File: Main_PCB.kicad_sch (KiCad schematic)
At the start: 5 parts

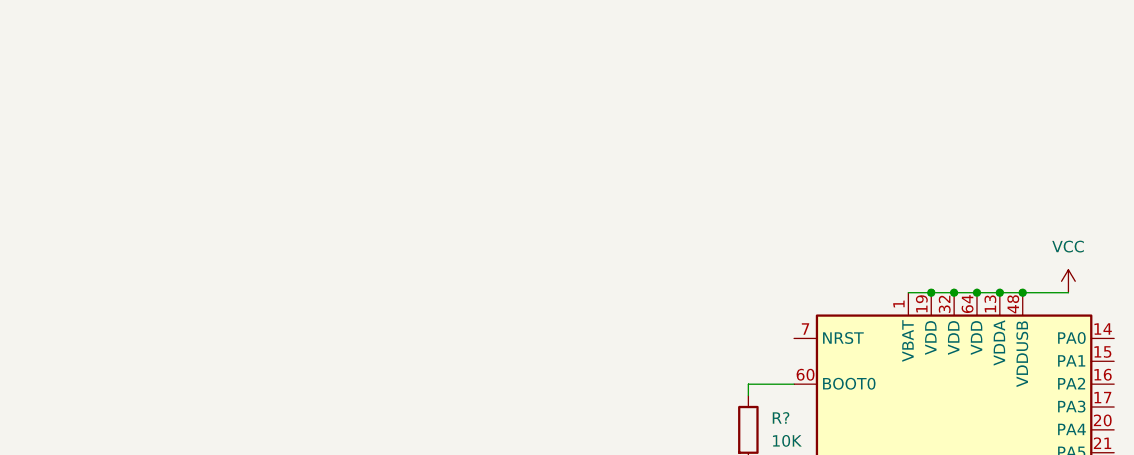
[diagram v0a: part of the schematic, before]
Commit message: started microcontroller pcb added lora, EEPROM, ArduinoHeaders and OUTPUTPINS
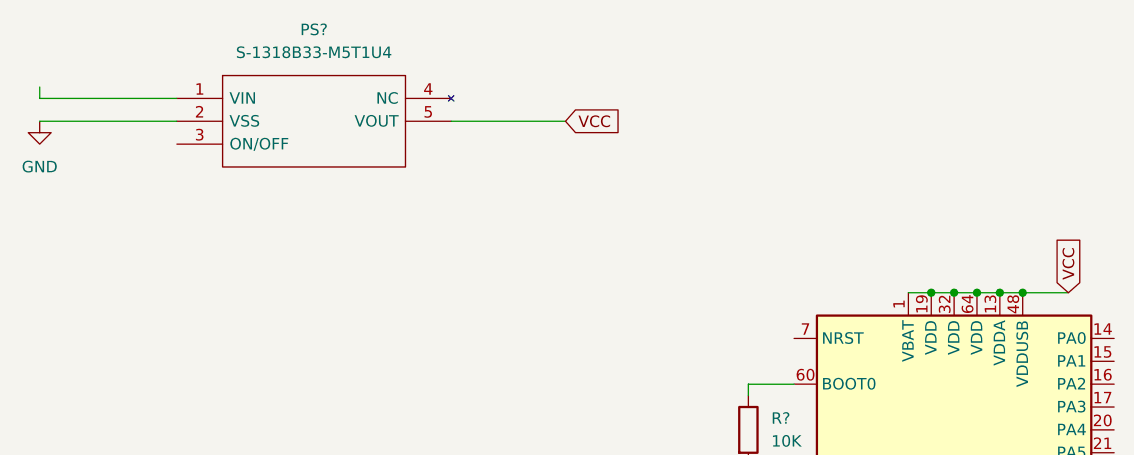
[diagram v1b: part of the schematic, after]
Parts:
- added PS?: S-1318B33-M5T1U4, SOT95P275X130-5N, symbol S-1318B33-M5T1U4:S-1318B33-M5T1U4
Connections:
- net GND: now also PS?.2 (VSS)
- net VCC: now also PS?.5 (VOUT)
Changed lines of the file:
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@@
   (junction (at 154.94 146.05) (diameter 0.9144) (color 0 0 0 0))
   (junction (at 157.48 54.61) (diameter 0.9144) (color 0 0 0 0))
+  (wire (pts (xy 48.26 31.75) (xy 48.26 33.02))
+    (stroke (width 0) (type default) (color 0 0 0 0))
+  )
+  (wire (pts (xy 48.26 33.02) (xy 63.5 33.02))
+    (stroke (width 0) (type default) (color 0 0 0 0))
+  )
+  (wire (pts (xy 63.5 35.56) (xy 48.26 35.56))
+    (stroke (width 0) (type default) (color 0 0 0 0))
+  )
+  (wire (pts (xy 93.98 35.56) (xy 106.68 35.56))
+    (stroke (width 0) (type default) (color 0 0 0 0))
+  )
   (wire (pts (xy 115.57 138.43) (xy 115.57 146.05))
     (stroke (width 0) (type solid) (color 0 0 0 0))
@@
     (stroke (width 0) (type solid) (color 0 0 0 0))
   )
-  (symbol (lib_id "power:VCC") (at 162.56 54.61 0) (unit 1)
-    (in_bom yes) (on_board yes) (fields_autoplaced)
-    (property "Reference" "#PWR?" (id 0) (at 162.56 58.42 0)
-      (effects (font (size 1.27 1.27)) hide)
-    )
-    (property "Value" "VCC" (id 1) (at 162.56 49.53 0))
-    (property "Footprint" "" (id 2) (at 162.56 54.61 0)
-      (effects (font (size 1.27 1.27)) hide)
-    )
-    (property "Datasheet" "" (id 3) (at 162.56 54.61 0)
+  (global_label "VCC" (shape input) (at 106.68 35.56 0) (fields_autoplaced)
+    (effects (font (size 1.27 1.27)) (justify left))
+    (property "Intersheet References" "${INTERSHEET_REFS}" (id 0) (at 112.7217 35.4806 0)
+      (effects (font (size 1.27 1.27)) (justify left) hide)
+    )
+  )
+  (global_label "VCC" (shape input) (at 162.56 54.61 90) (fields_autoplaced)
+    (effects (font (size 1.27 1.27)) (justify left))
+    (property "Intersheet References" "${INTERSHEET_REFS}" (id 0) (at 162.4806 48.5683 90)
+      (effects (font (size 1.27 1.27)) (justify left) hide)
+    )
+  )
+  (symbol (lib_id "power:GND") (at 48.26 35.56 0) (unit 1)
+    (in_bom yes) (on_board yes) (fields_autoplaced)
+    (property "Reference" "#PWR?" (id 0) (at 48.26 41.91 0)
+      (effects (font (size 1.27 1.27)) hide)
+    )
+    (property "Value" "GND" (id 1) (at 48.26 40.64 0))
+    (property "Footprint" "" (id 2) (at 48.26 35.56 0)
+      (effects (font (size 1.27 1.27)) hide)
+    )
+    (property "Datasheet" "" (id 3) (at 48.26 35.56 0)
       (effects (font (size 1.27 1.27)) hide)
     )
@@
     (pin "1")
     (pin "2")
+  )
+  (symbol (lib_id "S-1318B33-M5T1U4:S-1318B33-M5T1U4") (at 63.5 33.02 0) (unit 1)
+    (in_bom yes) (on_board yes) (fields_autoplaced)
+    (property "Reference" "PS?" (id 0) (at 78.74 25.4 0))
+    (property "Value" "S-1318B33-M5T1U4" (id 1) (at 78.74 27.94 0))
+    (property "Footprint" "SOT95P275X130-5N" (id 2) (at 90.17 30.48 0)
+      (effects (font (size 1.27 1.27)) (justify left) hide)
+    )
+    (property "Datasheet" "https://componentsearchengine.com/Datasheets/1/S-1318B33-M5T1U4.pdf" (id 3) (at 90.17 33.02 0)
+      (effects (font (size 1.27 1.27)) (justify left) hide)
+    )
+    (property "Description" "LDO Voltage Regulators 5.5V Input 100mA 95 nA 3.3V Output" (id 4) (at 90.17 35.56 0)
+      (effects (font (size 1.27 1.27)) (justify left) hide)
+    )
+    (property "Height" "1.3" (id 5) (at 90.17 38.1 0)
+      (effects (font (size 1.27 1.27)) (justify left) hide)
+    )
+    (property "Manufacturer_Name" "ABLIC Inc." (id 6) (at 90.17 40.64 0)
+      (effects (font (size 1.27 1.27)) (justify left) hide)
+    )
+    (property "Manufacturer_Part_Number" "S-1318B33-M5T1U4" (id 7) (at 90.17 43.18 0)
+      (effects (font (size 1.27 1.27)) (justify left) hide)
+    )
+    (property "Mouser Part Number" "628-S-1318B33-M5T1U4" (id 8) (at 90.17 45.72 0)
+      (effects (font (size 1.27 1.27)) (justify left) hide)
+    )
+    (property "Mouser Price/Stock" "https://www.mouser.com/Search/Refine.aspx?Keyword=628-S-1318B33-M5T1U4" (id 9) (at 90.17 48.26 0)
+      (effects (font (size 1.27 1.27)) (justify left) hide)
+    )
+    (property "Arrow Part Number" "" (id 10) (at 90.17 50.8 0)
+      (effects (font (size 1.27 1.27)) (justify left) hide)
+    )
+    (property "Arrow Price/Stock" "" (id 11) (at 90.17 53.34 0)
+      (effects (font (size 1.27 1.27)) (justify left) hide)
+    )
+    (pin "1")
+    (pin "2")
+    (pin "3")
+    (pin "4")
+    (pin "5")
   )
   (symbol (lib_id "MCU_ST_STM32L4:STM32L476RGTx") (at 149.86 100.33 0) (unit 1)
@@
       (reference "#PWR?") (unit 1) (value "GND") (footprint "")
     )
-    (path "/3cdf3227-f30a-4495-ac8b-0d36e0f57fd9"
-      (reference "#PWR?") (unit 1) (value "VCC") (footprint "")
-    )
     (path "/4c2bd4ea-05fe-490a-aef5-37b9aa28a49f"
       (reference "#PWR?") (unit 1) (value "GND") (footprint "")
     )
     (path "/71f3acb8-f249-4477-8678-d418f3c6a7d2"
+      (reference "#PWR?") (unit 1) (value "GND") (footprint "")
+    )
+    (path "/7621adb7-fe8e-4a06-9c81-43b3d705b253"
       (reference "#PWR?") (unit 1) (value "GND") (footprint "")
     )
@@
       (reference "C?") (unit 1) (value "4pF") (footprint "Capacitor_SMD:C_0603_1608Metric_Pad1.08x0.95mm_HandSolder")
     )
+    (path "/7fb52c71-aeae-4a20-8c17-b92ca4f2d7cf"
+      (reference "PS?") (unit 1) (value "S-1318B33-M5T1U4") (footprint "SOT95P275X130-5N")
+    )
     (path "/f64992af-738a-4402-854b-85b02260bd48"

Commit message: fixed microcontroller
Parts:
- added A?: Arduino_UNO_R3, Module:Arduino_UNO_R3, symbol MCU_Module:Arduino_UNO_R3
- added C? (x2): 100nF, symbol Device:C
- added IC?: 24AA64T-I_OT, SOT95P270X145-5N, symbol 24AA64T-I_OT:24AA64T-I_OT
- added IC?: TCN75AVUA713-VAO, SOP65P490X110-8N, symbol TCN75AVUA713-VAO:TCN75AVUA713-VAO
- added J?: Conn_02x03_Odd_Even, symbol Connector_Generic:Conn_02x03_Odd_Even
- added J?: Conn_Coaxial, symbol Connector:Conn_Coaxial
- added LED?: IN-P55TATRGB, INP55TATRGB, symbol IN-P55TATRGB:IN-P55TATRGB
- added R1, R?: 0R, symbol Device:R
- added R?: 4.7KR, symbol Device:R
- added U?: LTR-329ALS-01, LTR329ALS01, symbol LTR-329ALS-01:LTR-329ALS-01
- added U?: RFM95W-868S2, symbol RF_Module:RFM95W-868S2
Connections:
- net GND: now also A?.29 (GND), A?.6 (GND), A?.7 (GND), C?.1, C?.1, IC?.2 (VSS), IC?.4 (GND), IC?.5 (A2), IC?.6 (A1), J?.1 (Pin_1), J?.2 (Ext), U?.1 (GND), U?.10 (GND), U?.2 (GND), U?.8 (GND)
- net VCC: now also A?.4 (3V3), C?.2, C?.2, IC?.4 (VCC), IC?.7 (A0), IC?.8 (VDD), J?.2 (Pin_2), R?.1, U?.1 (VDD), U?.13 (3.3V)
- net OSC32_IN: now reaches C?.1, U?.3 (PC14), Y?.1
- net OSC32_OUT: now reaches C?.1, U?.4 (PC15), Y?.2
- net VBAT: now reaches PS?.1 (VIN)
- net VBAT: now also R1.1
- net at PS?.3 (ON/OFF): now also R1.2
- net SPI_LORA_NSS: now reaches U?.14 (PA0)
- net SPI_LORA_NSS: now also A?.9 (A0), U?.5 (NSS)
- net Lora-Reset: now reaches U?.15 (PA1)
- net Lora-Reset: now also A?.10 (A1), R?.2
- net SPI_LORA_SCK: now reaches U?.21 (PA5)
- net SPI_LORA_SCK: now also A?.28 (D13), U?.4 (SCK)
- net SPI_LORA_MISO: now reaches U?.22 (PA6)
- net SPI_LORA_MISO: now also A?.27 (D12), U?.2 (MISO)
- net SPI_LORA_MOSI: now reaches U?.23 (PA7)
- net SPI_LORA_MOSI: now also A?.26 (D11), U?.3 (MOSI)
- net IC2_MoistureSensor_SCL2: now reaches U?.34 (PB13)
- net IC2_MoistureSensor_SCL2: now also J?.5 (Pin_5)
- net IC2_MoistureSensor_SDA2: now reaches U?.35 (PB14)
- net IC2_MoistureSensor_SDA2: now also J?.6 (Pin_6)
- net LORA_DIO0: now reaches U?.43 (PA10)
- net LORA_DIO0: now also A?.17 (D2), U?.14 (DIO0)
- net LORA_DIO1: now reaches U?.55 (PB3)
- net LORA_DIO1: now also A?.18 (D3), U?.15 (DIO1)
- net I2C_EEPROM_SDA: now reaches U?.59 (PB7)
- net I2C_EEPROM_SDA: now also IC?.3 (SDA)
- net I2C_EEPROM_SCL: now reaches U?.61 (PB8)
- net I2C_EEPROM_SCL: now also IC?.1 (SCL)
- net IC2_MoistureSensor_SCL1: now reaches U?.8 (PC0)
- net IC2_MoistureSensor_SCL1: now also IC?.2 (SCL), J?.3 (Pin_3), U?.4 (SCL)
- net IC2_MoistureSensor_SDA1: now reaches U?.9 (PC1)
- net IC2_MoistureSensor_SDA1: now also IC?.1 (SDA), J?.4 (Pin_4), U?.3 (SDA)
- new net: J?.1 (In), U?.9 (ANT)
- new net: R?.1, R?.2, U?.6 (RESET)
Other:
- note added: "ARDUINO HEADERS"
- note added: "Cystal"
- note added: "EEPROM"
- note added: "LICHTSENSOR_MAIN_BOARD"
- note added: "LORA"
- note added: "OUTPUT_PINS_MOISTURE"
- note added: "TEMPERATUURSENSOR_MAIN_BOARD"
- note added: "Voeding"
- moved on the sheet: C?, PS?, R?, U?, Y?

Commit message: added connector for moisture sensor + connected arduino header 2 microcontroller
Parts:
- added R? (x3): 470R, symbol Device:R
- gave numbers to parts that had none: 1
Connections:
- net GND: now also LED?.1 (CATHODE_BLUE), LED?.2 (CATHODE_RED), LED?.3 (CATHODE_GREEN)
- net IC2_MoistureSensor_SCL1: now also A?.14 (SCL/A5), A?.32 (SCL/A5)
- net IC2_MoistureSensor_SDA1: now also A?.13 (SDA/A4), A?.31 (SDA/A4)
- net VCC: now also A?.2 (IOREF), A?.30 (AREF)
- net at LED?.4 (ANODE_GREEN): now also R?.2
- net at LED?.5 (ANODE_RED): now also R?.2
- net at LED?.6 (ANODE_BLUE): now also R?.2
- net D1_TX: now reaches U?.16 (PA2)
- net D1_TX: now also A?.16 (D1/TX)
- net D0_TX: now reaches U?.17 (PA3)
- net D0_TX: now also A?.15 (D0/RX)
- net A2: now reaches U?.20 (PA4)
- net A2: now also A?.11 (A2)
- net A3: now reaches U?.26 (PB0)
- net A3: now also A?.12 (A3)
- net D6: now reaches U?.29 (PB10)
- net D6: now also A?.21 (D6)
- net D9: now reaches U?.38 (PC7)
- net D9: now also A?.24 (D9)
- net D7: now reaches U?.41 (PA8)
- net D7: now also A?.22 (D7)
- net D8: now reaches U?.42 (PA9)
- net D8: now also A?.23 (D8)
- net D5: now reaches U?.56 (PB4)
- net D5: now also A?.20 (D5)
- net D4: now reaches U?.57 (PB5)
- net D4: now also A?.19 (D4)
- net D10: now reaches U?.58 (PB6)
- net D10: now also A?.25 (D10)
- net Reset: now reaches U?.7 (NRST)
- net Reset: now also A?.3 (~{RESET})
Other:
- note added: "INDICATIE_LED"
- note added: "Voeding LDO"
- note removed: "Voeding"
- moved on the sheet: A?, C?, IC?, J1, J?, LED?, PS?, R1, R?, U?, Y?

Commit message: added battery holder and swd programming port
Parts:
- removed LED?: IN-P55TATRGB, INP55TATRGB, symbol IN-P55TATRGB:IN-P55TATRGB
- removed R? (x3): 470R, symbol Device:R
- added F1: Fuse, Fuse:Fuse_0603_1608Metric_Pad1.05x0.95mm_HandSolder, symbol Device:Fuse
- added JP1: 20021521-00010T1LF, 20021521-00010T1LF:20021521-00010T1LF, symbol SWD_header:20021521-00010T1LF
- added U3: Dual_AA, Dual_AA:Dual_AA, symbol New_Library:Dual_AA
- gave numbers to parts that had none: 16
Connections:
- net GND: now also JP1.3, JP1.5, JP1.9, U3.3 (-bat1), U3.4 (-bat2)
- net LORA_DIO1: now also U4.28 (PB2); no longer U4.55 (PB3)
- net Reset: now also JP1.10
- net VBAT: now also F1.1
- net VCC: now also JP1.1
- net SWDIO: now reaches U4.46 (PA13)
- net SWDIO: now also JP1.2
- net SWCLK: now reaches U4.49 (PA14)
- net SWCLK: now also JP1.4
- new net: F1.2, U3.1 (+bat1), U3.2 (+bat2)
- new net SWO: JP1.6, U4.55 (PB3)
- no-connect marks 0 -> 3
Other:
- note added: "battery holder"
- note added: "swd programming port"
- note removed: "INDICATIE_LED"

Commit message: assigned footprints
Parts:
- added C10, C11, C12, C13, C14, C15, C5, C6, C7, C8, C9, C?: 100nF, Capacitor_SMD:C_0603_1608Metric_Pad1.08x0.95mm_HandSolder, symbol Device:C
- C1, C2: footprint (none) -> Capacitor_SMD:C_0603_1608Metric_Pad1.08x0.95mm_HandSolder
- IC1: footprint SOP65P490X110-8N -> TCN75AVUA713-VAO:SOP65P490X110-8N
- IC2: footprint SOT95P270X145-5N -> 24AA64T-I_OT:SOT95P270X145-5N
- J2: footprint (none) -> Connector_IDC:IDC-Header_2x03_P2.54mm_Vertical
- PS1: footprint SOT95P275X130-5N -> S-1318B33:SOT95P275X130-5N
- R1, R2, R3, R7: footprint (none) -> Resistor_SMD:R_0603_1608Metric_Pad0.98x0.95mm_HandSolder
- U1: footprint LTR329ALS01 -> KiCad:LTR329ALS01
- U2: footprint (none) -> RFM95W-868S2:XCVR_RFM95W-868S2
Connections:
- net GND: now also C10.1, C11.1, C12.1, C13.1, C14.1, C15.1, C5.1, C6.1, C7.1, C8.1, C9.1, C?.1
- net VBAT: now also C14.2
- net VCC: now also C10.2, C11.2, C12.2, C13.2, C15.2, C5.2, C6.2, C7.2, C8.2, C9.2, C?.2
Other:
- moved on the sheet: C3, C4, Y1

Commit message: did alot of the routing and pcb layout
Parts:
- removed A1: Arduino_UNO_R3, Module:Arduino_UNO_R3, symbol MCU_Module:Arduino_UNO_R3
- removed U3: Dual_AA, Dual_AA:Dual_AA, symbol New_Library:Dual_AA
- added C17, C18, C19, C20: 100nF, Capacitor_SMD:C_0805_2012Metric_Pad1.18x1.45mm_HandSolder, symbol Device:C
- added D1: LED, LED_SMD:LED_0805_2012Metric_Pad1.15x1.40mm_HandSolder, symbol Device:LED
- added F2: Fuse, Fuse:Fuse_0603_1608Metric_Pad1.05x0.95mm_HandSolder, symbol Device:Fuse
- added J3: USB_C_Receptacle_USB2.0, Connector_USB:USB_C_Receptacle_HRO_TYPE-C-31-M-12, symbol Connector:USB_C_Receptacle_USB2.0
- added J4: Conn_01x03_Male, Connector_PinHeader_2.54mm:PinHeader_1x03_P2.54mm_Vertical, symbol Connector:Conn_01x03_Male
- added J? (x2): Conn_01x15_Female, symbol Connector:Conn_01x15_Female
- added PS2: S-1318B33-M5T1U4, S-1318B33:SOT95P275X130-5N, symbol S-1318B33-M5T1U4:S-1318B33-M5T1U4
- added R10, R6: 360R, Resistor_SMD:R_0603_1608Metric_Pad0.98x0.95mm_HandSolder, symbol Device:R
- added R11: 0R, Resistor_SMD:R_0603_1608Metric_Pad0.98x0.95mm_HandSolder, symbol Device:R
- added R12: 220k, Resistor_SMD:R_0603_1608Metric_Pad0.98x0.95mm_HandSolder, symbol Device:R
- added R13: 330k, Resistor_SMD:R_0603_1608Metric_Pad0.98x0.95mm_HandSolder, symbol Device:R
- added R4, R5: 5.1k, Resistor_SMD:R_0603_1608Metric_Pad0.98x0.95mm_HandSolder, symbol Device:R
- added R8, R9: 100k, Resistor_SMD:R_0603_1608Metric_Pad0.98x0.95mm_HandSolder, symbol Device:R
- added SW1, SW2: SW_Push, Button_Switch_SMD:SW_SPST_TL3342, symbol Switch:SW_Push
- added U3: 1013, 1013:1013, symbol 1013:1013
- added U5: ATECC508A-SSHDA-T, ATECC508A:ATECC508A-SSHDA-T, symbol ATECC508A:ATECC508A-SSHDA-T
- added U7: USBLC6-2SC6, Package_TO_SOT_SMD:SOT-23-6, symbol Power_Protection:USBLC6-2SC6
- C13, C2: footprint Capacitor_SMD:C_0603_1608Metric_Pad1.08x0.95mm_HandSolder -> Capacitor_SMD:C_0805_2012Metric_Pad1.18x1.45mm_HandSolder
- J1: footprint (none) -> Connector_Coaxial:SMA_Amphenol_901-144_Vertical
- R7: value 10K -> 360R
- U1: footprint KiCad:LTR329ALS01 -> LTR-329ALS:LTR329ALS01
- gave numbers to parts that had none: 1
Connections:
- net A3: now also J?.7 (Pin_7)
- net D0_TX: now also J?.9 (Pin_9)
- net D10: now also J?.1 (Pin_1)
- net D1_TX: now also J?.10 (Pin_10)
- net D4: now also R10.2
- net D5: now also J?.6 (Pin_6)
- net D6: now also J?.5 (Pin_5)
- net D7: now also J?.4 (Pin_4)
- net D8: now also J?.3 (Pin_3)
- net D9: now also J?.2 (Pin_2)
- net GND: now also C13.2, C2.2, IC2.5 (WP), C17.2, C18.2, C19.2, C20.2, D1.1 (K), J3.A1 (GND), J3.A12 (GND), J3.B1 (GND), J3.B12 (GND), J3.S1 (SHIELD), J?.14 (Pin_14), J?.15 (Pin_15), PS2.2 (VSS), R13.2, R4.2, R5.2, SW1.1, SW2.1, U3.3, U3.4, U5.4 (GND), U7.2 (GND); no longer C13.1, C2.1, R7.2
- net IC2_MoistureSensor_SCL1: now also IC2.1 (SCL), J?.11 (Pin_11), U5.6 (SCL)
- net IC2_MoistureSensor_SCL2: now also J?.10 (Pin_10)
- net IC2_MoistureSensor_SDA1: now also IC2.3 (SDA), J?.12 (Pin_12), U5.5 (SDA)
- net IC2_MoistureSensor_SDA2: now also J?.9 (Pin_9)
- net LORA_DIO0: now also J?.13 (Pin_13)
- net LORA_DIO1: now also J?.14 (Pin_14)
- net Reset: now also C2.1, J?.13 (Pin_13), R6.2, R8.2
- net SPI_LORA_MISO: now also J?.5 (Pin_5)
- net SPI_LORA_MOSI: now also J?.4 (Pin_4)
- net SPI_LORA_NSS: now also J?.3 (Pin_3)
- net SPI_LORA_SCK: now also J?.6 (Pin_6)
- net VBAT: now also F2.1, J?.15 (Pin_15), R12.1
- net VCC: now also J4.2 (Pin_2), J?.1 (Pin_1), J?.2 (Pin_2), R8.1, R9.1, U5.8 (VCC); no longer C13.2, C15.2, C2.2, PS1.5 (VOUT)
- net PC2: now reaches U4.10 (PC2)
- net PC3: now reaches U4.11 (PC3)
- net PC13: now reaches U4.2 (PC13)
- net PC4: now reaches U4.24 (PC4)
- net PC5: now reaches U4.25 (PC5)
- net PB1: now reaches U4.27 (PB1)
- net PB11: now reaches U4.30 (PB11)
- net PB12: now reaches U4.33 (PB12)
- net PB15: now reaches U4.36 (PB15)
- net PC6: now reaches U4.37 (PC6)
- net PC8: now reaches U4.39 (PC8)
- net PC9: now reaches U4.40 (PC9)
- net USB-: now reaches U4.44 (PA11)
- net USB-: now also U7.3 (I/O2)
- net USB+: now reaches U4.45 (PA12)
- net USB+: now also U7.1 (I/O1)
- net PH0: now reaches U4.5 (PH0)
- net PA15: now reaches U4.50 (PA15)
- net PC10: now reaches U4.51 (PC10)
- net PC11: now reaches U4.52 (PC11)
- net PC12: now reaches U4.53 (PC12)
- net PD2: now reaches U4.54 (PD2)
- net PH1: now reaches U4.6 (PH1)
- net at R7.1: now also SW2.2; no longer U4.60 (BOOT0)
- net PB9: now reaches U4.62 (PB9)
- net at F1.2: now also U3.1
- net A2 renamed bat_voltage
- net bat_voltage: now also C13.1, J?.8 (Pin_8), R12.2, R13.1
- net I2C_EEPROM_SCL renamed PB8
- net PB8: now also J?.7 (Pin_7); no longer IC2.1 (SCL)
- net I2C_EEPROM_SDA renamed PB7
- net PB7: now also J?.8 (Pin_8); no longer IC2.3 (SDA)
- new net: D1.2 (A), R10.1
- new net: R6.1, SW1.2
- new net: J3.A5 (CC1), R4.1
- new net: J3.B5 (CC2), R5.1
- new net: F2.2, U3.2
- new net: PS2.3 (ON/OFF), R11.1
- new net +5V: C17.1, C19.1, J3.A4 (VBUS), J3.A9 (VBUS), J3.B4 (VBUS), J3.B9 (VBUS), PS2.1 (VIN), R11.2, U7.5 (VBUS)
- new net D+: J3.A6 (D+), J3.B6 (D+), U7.6 (I/O1)
- new net D-: J3.A7 (D-), J3.B7 (D-), U7.4 (I/O2)
- new net battery: C15.2, J4.3 (Pin_3), PS1.5 (VOUT)
- new net boot0: C20.1, J?.12 (Pin_12), R7.2, R9.2, U4.60 (BOOT0)
- new net usb3v3: C18.1, J4.1 (Pin_1), PS2.5 (VOUT)
- no-connect marks 3 -> 5
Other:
- note added: "ATECC508A crypto coprocessor"
- note added: "ESD protection"
- note added: "battery voltage monitoring"
- note added: "usb input"
- note removed: "ARDUINO HEADERS"
- moved on the sheet: C1, C3, C4, F1, JP1, Y1

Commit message: finished pcb
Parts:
- removed J? (x2): Conn_01x15_Female, symbol Connector:Conn_01x15_Female
- added J5: Conn_01x08, Connector_JST:JST_EH_B8B-EH-A_1x08_P2.50mm_Vertical, symbol Connector_Generic:Conn_01x08
- added J6: Conn_01x08, Connector_JST:JST_EH_S8B-EH_1x08_P2.50mm_Horizontal, symbol Connector_Generic:Conn_01x08
- added U6: ST-Nucleo-L432KC, Module:ST-Nucleo-L432KC, symbol MCU_Module:ST-Nucleo-L432KC
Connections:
- net D0_TX: now also U6.2 (PA10)
- net D1_TX: now also U6.1 (PA9)
- net D9: now also U6.12 (PA8); no longer U4.38 (PC7)
- net GND: now also J5.1 (Pin_1), J6.8 (Pin_8), U6.4 (GND)
- net IC2_MoistureSensor_SCL1: now also J5.5 (Pin_5), J6.4 (Pin_4), U6.25 (PA7)
- net IC2_MoistureSensor_SCL2: now also U6.8 (PB6)
- net IC2_MoistureSensor_SDA1: now also J5.6 (Pin_6), J6.3 (Pin_3), U6.15 (PB4)
- net IC2_MoistureSensor_SDA2: now also U6.7 (PB7)
- net LORA_DIO0: now also U6.20 (PA1)
- net LORA_DIO1: now also U6.21 (PA3)
- net Lora-Reset: now also U6.22 (PA4)
- net Reset: now also U6.3 (NRST)
- net SPI_LORA_MISO: now also U6.13 (PA11)
- net SPI_LORA_MOSI: now also U6.5 (PA12)
- net SPI_LORA_NSS: now also U6.6 (PB0)
- net SPI_LORA_SCK: now also U6.23 (PA5)
- net VBAT: now also J5.8 (Pin_8), J6.1 (Pin_1)
- net VCC: now also J5.2 (Pin_2), J6.7 (Pin_7), U6.17 (3V3)
- net bat_voltage: now also U6.19 (PA0)
- net battery: now also J5.7 (Pin_7), J6.2 (Pin_2)
- net A3: no longer names the net of U4.26 (PB0)
- net D10: no longer names the net of U4.58 (PB6)
- net D4 renamed LED
- net LED: now also J5.4 (Pin_4), J6.5 (Pin_5), U6.16 (PB3)
- net D5: no longer names the net of U4.56 (PB4)
- net D6: no longer names the net of U4.29 (PB10)
- net D7: no longer names the net of U4.41 (PA8)
- net D8: no longer names the net of U4.42 (PA9)
- net PB1: no longer names the net of U4.27 (PB1)
- net PB11: no longer names the net of U4.30 (PB11)
- net PB12: no longer names the net of U4.33 (PB12)
- net PB15: no longer names the net of U4.36 (PB15)
- net PB7: no longer names the net of U4.59 (PB7)
- net PB8: no longer names the net of U4.61 (PB8)
- net PB9: no longer names the net of U4.62 (PB9)
- net PC10: no longer names the net of U4.51 (PC10)
- net PC11: no longer names the net of U4.52 (PC11)
- net PC12: no longer names the net of U4.53 (PC12)
- net PC13: no longer names the net of U4.2 (PC13)
- net PC2: no longer names the net of U4.10 (PC2)
- net PC3: no longer names the net of U4.11 (PC3)
- net PC4: no longer names the net of U4.24 (PC4)
- net PC5: no longer names the net of U4.25 (PC5)
- net PC6: no longer names the net of U4.37 (PC6)
- net PC8: no longer names the net of U4.39 (PC8)
- net PC9: no longer names the net of U4.40 (PC9)
- net PD2: no longer names the net of U4.54 (PD2)
- net PH0: no longer names the net of U4.5 (PH0)
- net PH1: no longer names the net of U4.6 (PH1)
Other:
- moved on the sheet: J4
